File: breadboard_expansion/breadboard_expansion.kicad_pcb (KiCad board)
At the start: 2 copper layers, 27.9 x 53.3 mm, 4 parts, among them J1 Conn_01x02_Male, J2 Conn_01x02_Male, J3 Conn_01x02_Male, J4 Conn_01x02_Male

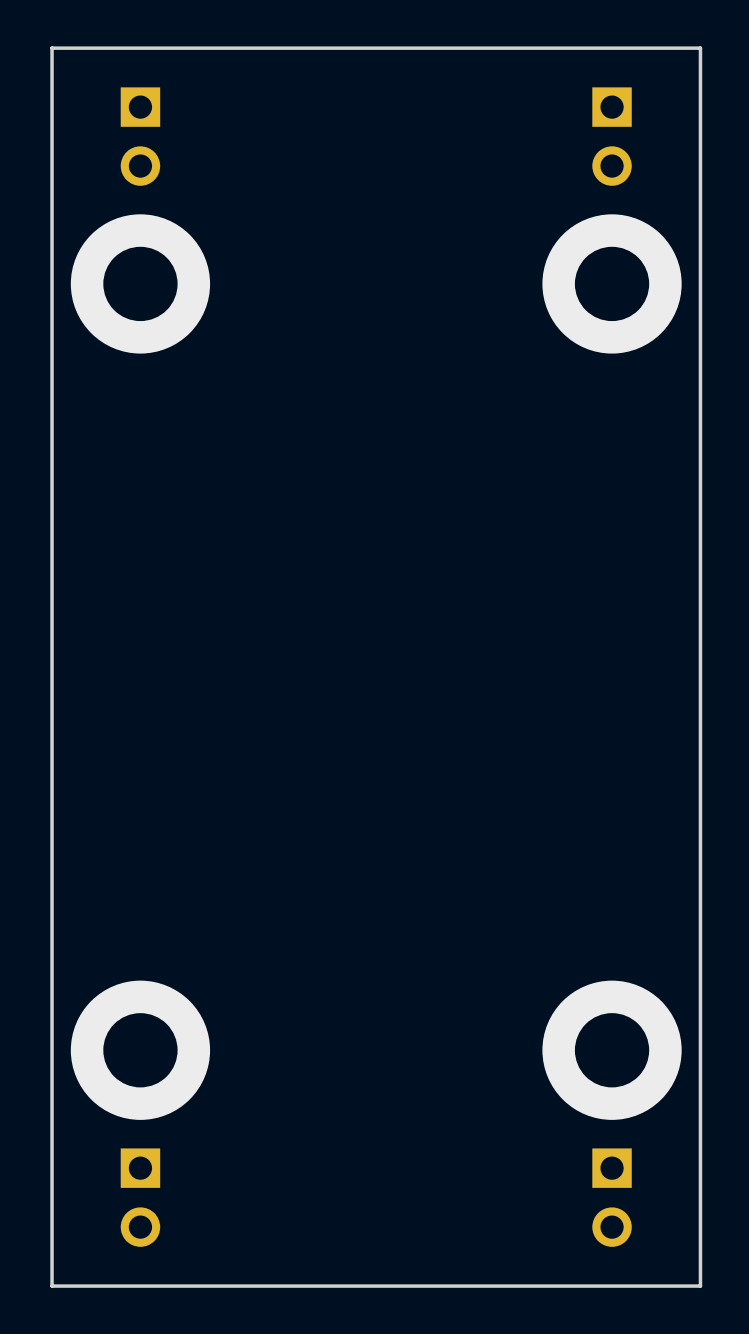
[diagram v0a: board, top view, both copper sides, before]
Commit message: Add voltage labels.
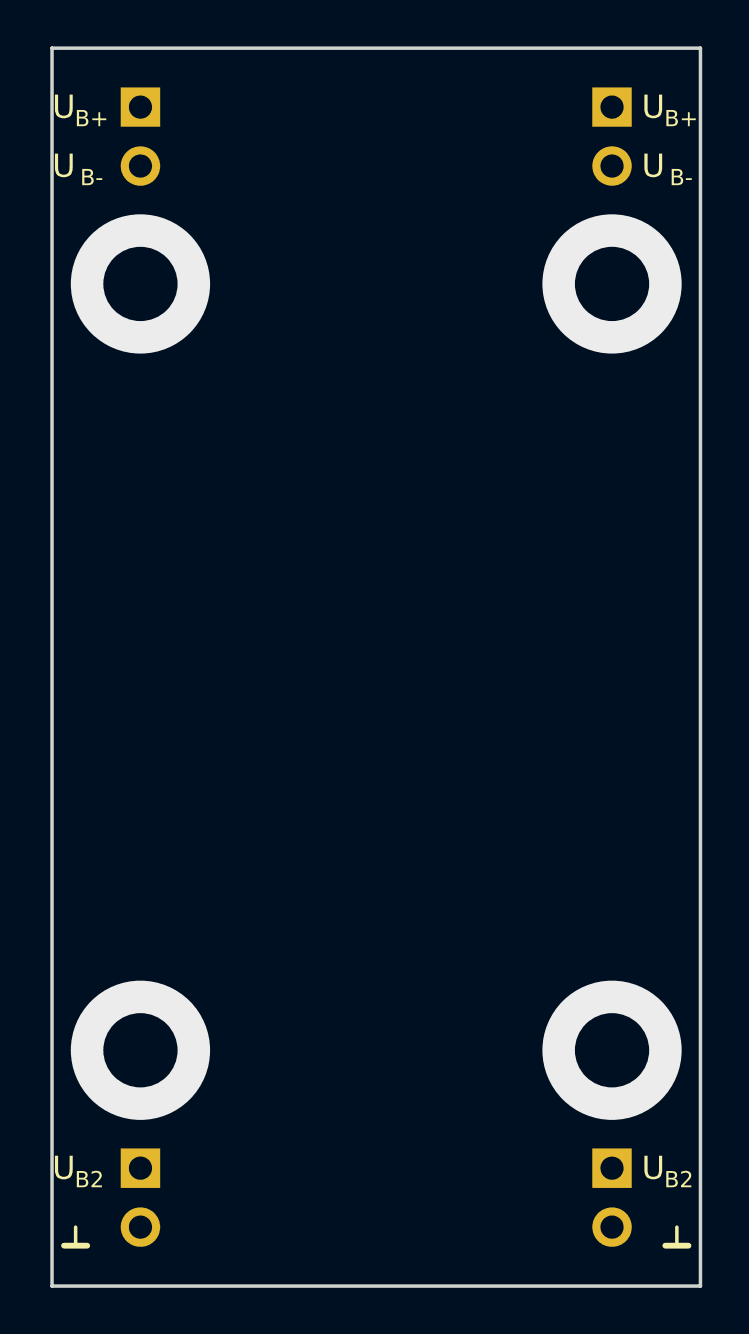
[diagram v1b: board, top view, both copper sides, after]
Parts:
- added REF**: Text_U_B+_Silkscreen, Symbol-emt:Text_U_B+_Silkscreen, F.Cu at (75.4, 91.4)
- added REF**: Text_U_B-_Silkscreen, Symbol-emt:Text_U_B-_Silkscreen, F.Cu at (75.4, 94.0)
- added REF**: Text_U_B2_Silkscreen, Symbol-emt:Text_U_B2_Silkscreen, F.Cu at (75.4, 137.2)
- added REF**: Symbol_GND_Silkscreen, Symbol-emt:Symbol_GND_Silkscreen, F.Cu at (75.9, 139.7)
- added REF**: Text_U_B+_Silkscreen, Symbol-emt:Text_U_B+_Silkscreen, F.Cu at (100.8, 91.4)
- added REF**: Text_U_B-_Silkscreen, Symbol-emt:Text_U_B-_Silkscreen, F.Cu at (100.8, 94.0)
- added REF**: Text_U_B2_Silkscreen, Symbol-emt:Text_U_B2_Silkscreen, F.Cu at (100.8, 137.2)
- added REF**: Symbol_GND_Silkscreen, Symbol-emt:Symbol_GND_Silkscreen, F.Cu at (101.9, 139.7)
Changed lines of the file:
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@@
     (tracks 4)
     (zones 0)
-    (modules 4)
+    (modules 12)
     (nets 5)
   )
@@
     )
   )
+  (module Symbol-emt:Text_U_B+_Silkscreen (layer F.Cu)
+    (at 75.438 91.44)
+    (descr "Voltage Label Betriebsspannung")
+    (tags "Voltage Label Betriebsspannung")
+    (attr virtual)
+    (fp_text reference REF** (at 0 1.65) (layer F.SilkS) hide
+      (effects (font (size 1 1) (thickness 0.15)))
+    )
+    (fp_text value Text_U_B+_Silkscreen (at 0 -1.5) (layer F.Fab) hide
+      (effects (font (size 1 1) (thickness 0.15)))
+    )
+    (fp_text user B+ (at 1.2 0.5) (layer F.SilkS)
+      (effects (font (size 0.7 0.7) (thickness 0.1)))
+    )
+    (fp_text user U (at 0 0) (layer F.SilkS)
+      (effects (font (size 1 1) (thickness 0.15)))
+    )
+  )
+  (module Symbol-emt:Text_U_B-_Silkscreen (layer F.Cu)
+    (at 75.438 93.98)
+    (descr "Voltage Label Betriebsspannung")
+    (tags "Voltage Label Betriebsspannung")
+    (attr virtual)
+    (fp_text reference REF** (at 0 1.65) (layer F.SilkS) hide
+      (effects (font (size 1 1) (thickness 0.15)))
+    )
+    (fp_text value Text_U_B-_Silkscreen (at 0 -1.5) (layer F.Fab) hide
+      (effects (font (size 1 1) (thickness 0.15)))
+    )
+    (fp_text user B- (at 1.2 0.5) (layer F.SilkS)
+      (effects (font (size 0.7 0.7) (thickness 0.1)))
+    )
+    (fp_text user U (at 0 0) (layer F.SilkS)
+      (effects (font (size 1 1) (thickness 0.15)))
+    )
+  )
+  (module Symbol-emt:Text_U_B2_Silkscreen (layer F.Cu)
+    (at 75.438 137.16)
+    (descr "Voltage Label Betriebsspannung")
+    (tags "Voltage Label Betriebsspannung")
+    (attr virtual)
+    (fp_text reference REF** (at 0 1.65) (layer F.SilkS) hide
+      (effects (font (size 1 1) (thickness 0.15)))
+    )
+    (fp_text value Text_U_B2_Silkscreen (at 0 -1.5) (layer F.Fab) hide
+      (effects (font (size 1 1) (thickness 0.15)))
+    )
+    (fp_text user B2 (at 1.1 0.5) (layer F.SilkS)
+      (effects (font (size 0.7 0.7) (thickness 0.1)))
+    )
+    (fp_text user U (at 0 0) (layer F.SilkS)
+      (effects (font (size 1 1) (thickness 0.15)))
+    )
+  )
+  (module Symbol-emt:Symbol_GND_Silkscreen (layer F.Cu)
+    (at 75.946 139.7)
+    (descr "Symbol GND")
+    (tags "Symbol GND")
+    (attr virtual)
+    (fp_text reference REF** (at 0 1.6) (layer F.SilkS) hide
+      (effects (font (size 1 1) (thickness 0.15)))
+    )
+    (fp_text value Symbol_GND_Silkscreen (at 0 -0.75) (layer F.Fab) hide
+      (effects (font (size 1 1) (thickness 0.15)))
+    )
+    (fp_line (start 0 0.8) (end 0 0) (layer F.SilkS) (width 0.15))
+    (fp_line (start -0.5 0.8) (end 0.5 0.8) (layer F.SilkS) (width 0.25))
+  )
+  (module Symbol-emt:Text_U_B+_Silkscreen (layer F.Cu)
+    (at 100.838 91.44)
+    (descr "Voltage Label Betriebsspannung")
+    (tags "Voltage Label Betriebsspannung")
+    (attr virtual)
+    (fp_text reference REF** (at 0 1.65) (layer F.SilkS) hide
+      (effects (font (size 1 1) (thickness 0.15)))
+    )
+    (fp_text value Text_U_B+_Silkscreen (at 0 -1.5) (layer F.Fab) hide
+      (effects (font (size 1 1) (thickness 0.15)))
+    )
+    (fp_text user B+ (at 1.2 0.5) (layer F.SilkS)
+      (effects (font (size 0.7 0.7) (thickness 0.1)))
+    )
+    (fp_text user U (at 0 0) (layer F.SilkS)
+      (effects (font (size 1 1) (thickness 0.15)))
+    )
+  )
+  (module Symbol-emt:Text_U_B-_Silkscreen (layer F.Cu)
+    (at 100.838 93.98)
+    (descr "Voltage Label Betriebsspannung")
+    (tags "Voltage Label Betriebsspannung")
+    (attr virtual)
+    (fp_text reference REF** (at 0 1.65) (layer F.SilkS) hide
+      (effects (font (size 1 1) (thickness 0.15)))
+    )
+    (fp_text value Text_U_B-_Silkscreen (at 0 -1.5) (layer F.Fab) hide
+      (effects (font (size 1 1) (thickness 0.15)))
+    )
+    (fp_text user B- (at 1.2 0.5) (layer F.SilkS)
+      (effects (font (size 0.7 0.7) (thickness 0.1)))
+    )
+    (fp_text user U (at 0 0) (layer F.SilkS)
+      (effects (font (size 1 1) (thickness 0.15)))
+    )
+  )
+  (module Symbol-emt:Text_U_B2_Silkscreen (layer F.Cu)
+    (at 100.838 137.16)
+    (descr "Voltage Label Betriebsspannung")
+    (tags "Voltage Label Betriebsspannung")
+    (attr virtual)
+    (fp_text reference REF** (at 0 1.65) (layer F.SilkS) hide
+      (effects (font (size 1 1) (thickness 0.15)))
+    )
+    (fp_text value Text_U_B2_Silkscreen (at 0 -1.5) (layer F.Fab) hide
+      (effects (font (size 1 1) (thickness 0.15)))
+    )
+    (fp_text user B2 (at 1.1 0.5) (layer F.SilkS)
+      (effects (font (size 0.7 0.7) (thickness 0.1)))
+    )
+    (fp_text user U (at 0 0) (layer F.SilkS)
+      (effects (font (size 1 1) (thickness 0.15)))
+    )
+  )
+  (module Symbol-emt:Symbol_GND_Silkscreen (layer F.Cu)
+    (at 101.854 139.7)
+    (descr "Symbol GND")
+    (tags "Symbol GND")
+    (attr virtual)
+    (fp_text reference REF** (at 0 1.6) (layer F.SilkS) hide
+      (effects (font (size 1 1) (thickness 0.15)))
+    )
+    (fp_text value Symbol_GND_Silkscreen (at 0 -0.75) (layer F.Fab) hide
+      (effects (font (size 1 1) (thickness 0.15)))
+    )
+    (fp_line (start 0 0.8) (end 0 0) (layer F.SilkS) (width 0.15))
+    (fp_line (start -0.5 0.8) (end 0.5 0.8) (layer F.SilkS) (width 0.25))
+  )
   (gr_line (start 102.87 88.9) (end 102.87 142.24) (layer Edge.Cuts) (width 0.15))
